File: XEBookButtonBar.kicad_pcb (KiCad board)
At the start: 2 copper layers, 90.5 x 12 mm, 7 parts

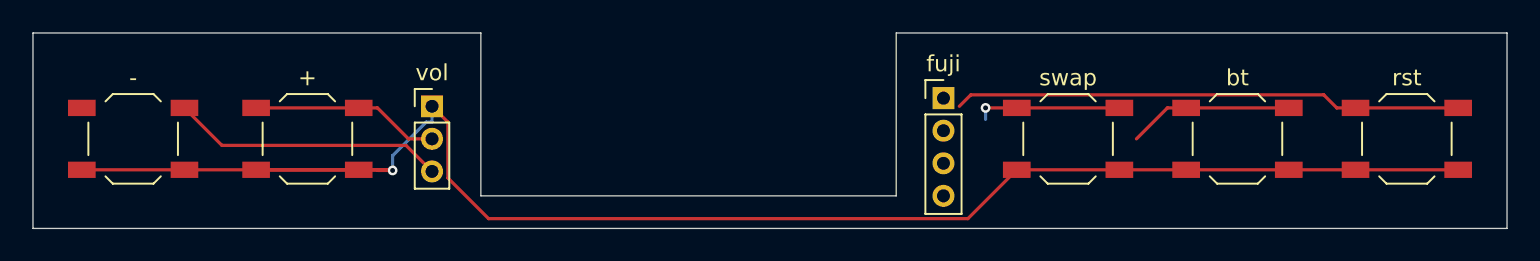
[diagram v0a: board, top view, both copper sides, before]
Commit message: Route J2's 4th pin and add JLCPCB fab package
Manual copper routing for J2's GND pin and the three re-numbered signal
pads is complete. Verified with kicad-cli pcb drc (full + schematic
parity): 0 unconnected pads, 0 shorts, only the two pre-existing
cosmetic lib_footprint_mismatch warnings.

Added Fab/ with gerbers, drill files (PTH/NPTH + maps), gerber job
file, a bundled Fab.zip for JLCPCB's bare-PCB upload, and JLCPCB-format
BOM/CPL covering the 5 SMD switches (J1/J2 are DNP -- cable wires are
soldered directly to those through-hole pins, no header part is
populated). The BOM's LCSC column is intentionally blank: no part
number for the TL3342 switch was ever recorded in this project.

Co-Authored-By: Claude Sonnet 5 <noreply@anthropic.com>
Claude-Session: https://claude.ai/code/session_01JYDshXZvRN7GDF7943FcwP
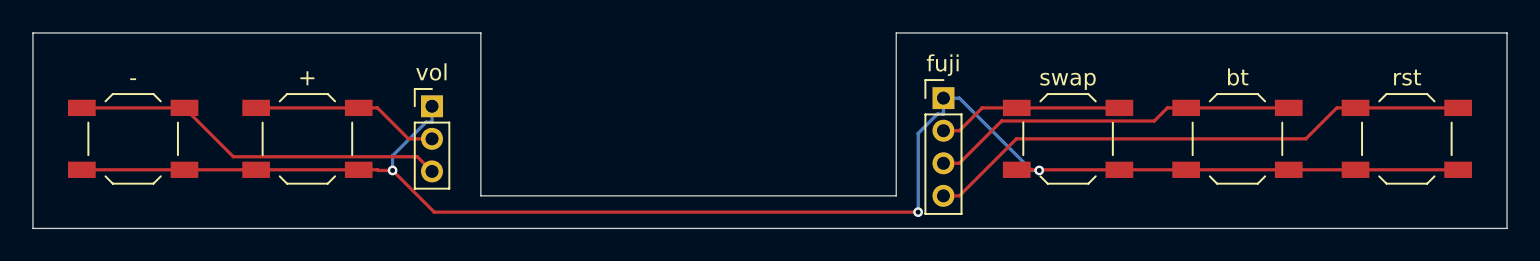
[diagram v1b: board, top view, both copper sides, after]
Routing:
- net Net-(J2-Pin_2): track 10.1 -> 22.6 mm
- net Net-(J1-Pin_3): track 16.8 -> 23.1 mm
- net Net-(J2-Pin_1): track 31.2 -> 33.8 mm
- net Net-(J2-Pin_3): track 8.92 -> 11.4 mm, vias 1 -> 0
- net GNDREF: track 101.8 -> 100.5 mm, vias 1 -> 3

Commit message: Sync schematic ref designators to PCB labels; regenerate fab package
Renamed schematic reference designators to match the PCB's functional
silkscreen labels (J1->vol, J2->fuji, SW3->swap, SW4->bt, SW6->rst),
and renamed SW1/SW2 from the DSN/JLC-hostile "-"/"+" to VolDWN/VolUP
in both schematic and PCB, so `-`/`+` no longer appear anywhere as a
literal reference designator (that character choice was silently
dropping ratsnest entries in Specctra DSN export/Freerouting and
likely breaking JLCPCB's BOM parser, since both treat bare +/- as
reserved tokens).

After the user ran Update PCB from Schematic and finished routing,
verified clean: ERC (only the pre-existing unrelated #PWR01 warning),
and `kicad-cli pcb drc --schematic-parity` reports 0 unconnected pads,
0 shorts, and 0 schematic-parity issues -- the previous 14 pre-existing
missing/extra-footprint warnings are resolved now that references
actually match. KiCad's own annotation pass appended "1" to each
custom reference during the update (e.g. fuji -> fuji1); harmless,
schematic and PCB agree on it consistently.

Regenerated Fab/ (gerbers, drill, gerber job, bundled Fab.zip, JLCPCB
BOM/CPL) against the routed board and current reference names.

Co-Authored-By: Claude Sonnet 5 <noreply@anthropic.com>
Claude-Session: https://claude.ai/code/session_01JYDshXZvRN7GDF7943FcwP
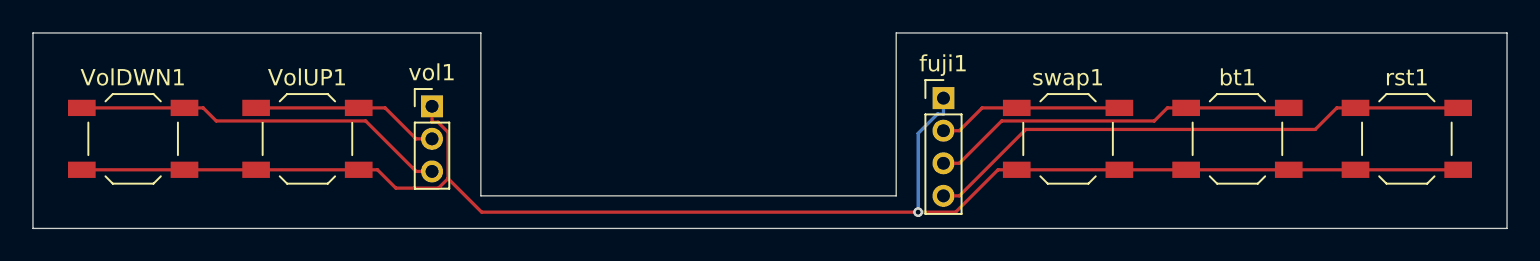
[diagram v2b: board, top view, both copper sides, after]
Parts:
- renumbered - to VolDWN1, + to VolUP1, bt to bt1, fuji to fuji1, rst to rst1, swap to swap1, vol to vol1
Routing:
- net GNDREF: track 100.5 -> 100.1 mm, vias 3 -> 1
